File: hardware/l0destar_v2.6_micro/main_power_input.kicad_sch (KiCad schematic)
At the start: 9 parts

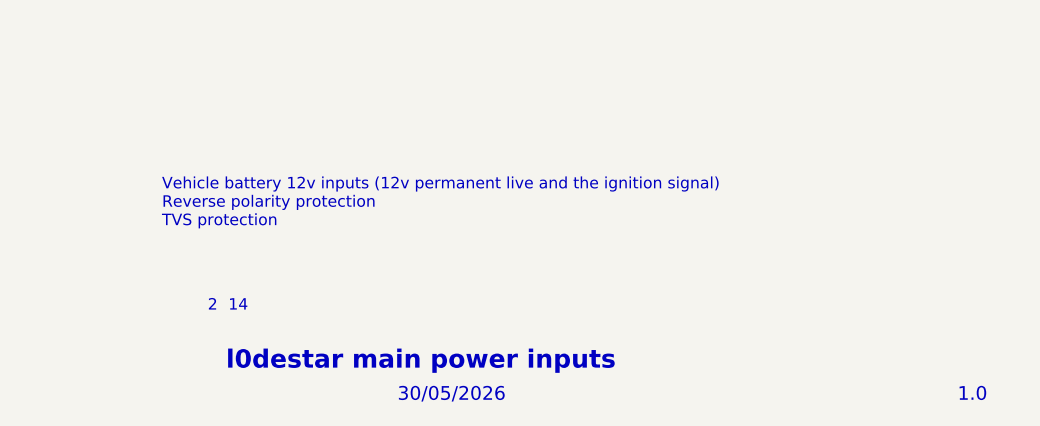
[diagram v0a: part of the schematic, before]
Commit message: update sheet annotations
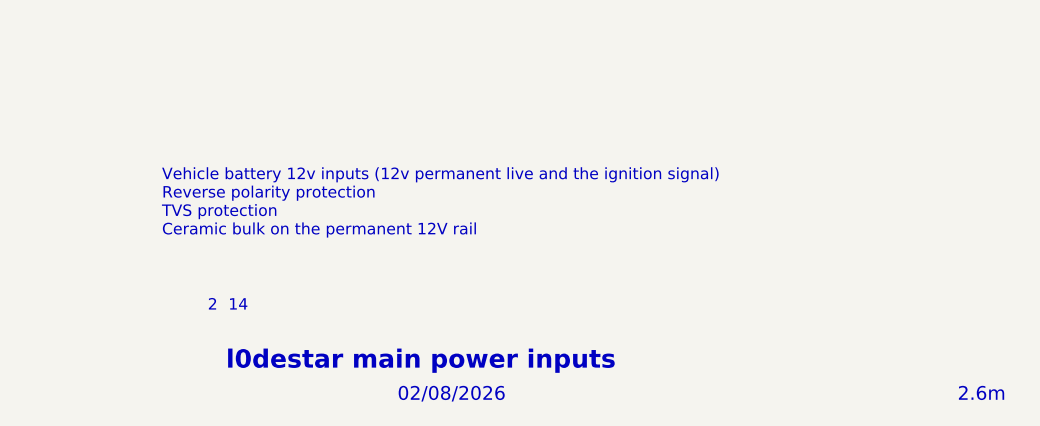
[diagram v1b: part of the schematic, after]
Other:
- note added: "02/08/2026"
- note added: "2.6m"
- note added: "Vehicle battery 12v inputs (12v permanent live and the ignition signal) Reverse polarity protection TVS protection Ceramic bulk on the permanent 12V rail"
- note removed: "1.0"
- note removed: "30/05/2026"
- note removed: "Vehicle battery 12v inputs (12v permanent live and the ignition signal) Reverse polarity protection TVS protection"
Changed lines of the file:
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@@
 	(generator_version "10.0")
 	(paper "A4")
-	(text "30/05/2026"
+	(text "02/08/2026"
 		(exclude_from_sim no)
 		(at 206.248 193.294 0)
@@
 		)
 	)
-	(text "Vehicle battery 12v inputs (12v permanent live and the ignition signal)\nReverse polarity protection\nTVS protection"
+	(text "Vehicle battery 12v inputs (12v permanent live and the ignition signal)\nReverse polarity protection\nTVS protection\nCeramic bulk on the permanent 12V rail"
 		(exclude_from_sim no)
 		(at 180.086 171.958 0)
@@
 		)
 	)
-	(text "1.0"
+	(text "2.6m"
 		(exclude_from_sim no)
 		(at 268.478 193.294 0)
